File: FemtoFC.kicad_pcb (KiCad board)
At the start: 4 copper layers, 15 x 56 mm, 61 parts, among them J1 Power in, J3 Micro_SD_Card, J4 Pyro 2, J5 Pyro 2, P1 USB_C_Plug_USB2.0, Q1 FDS9926A, Q2 FDS4953, Q3 NDT3055L, U1 USBLC6-2SC6, U2 3.3v REG, U3 ATSAMD21G18A-M, U4 W25Q128JVS, U5 LSM6DS3, U6 BMP280

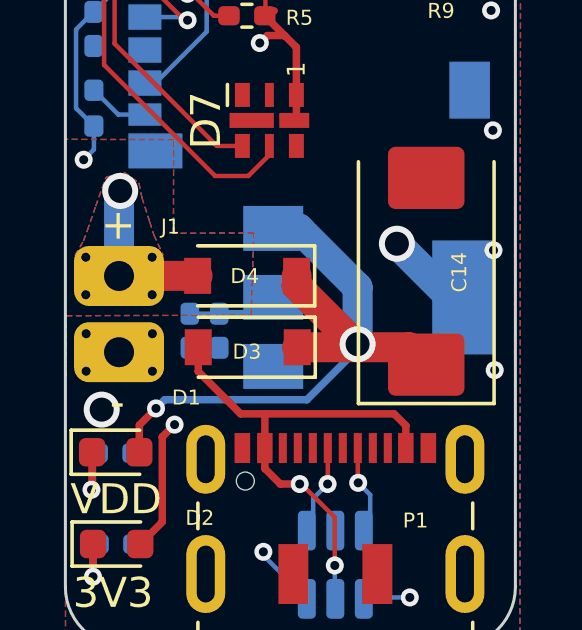
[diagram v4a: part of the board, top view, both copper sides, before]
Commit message: fixed ground short
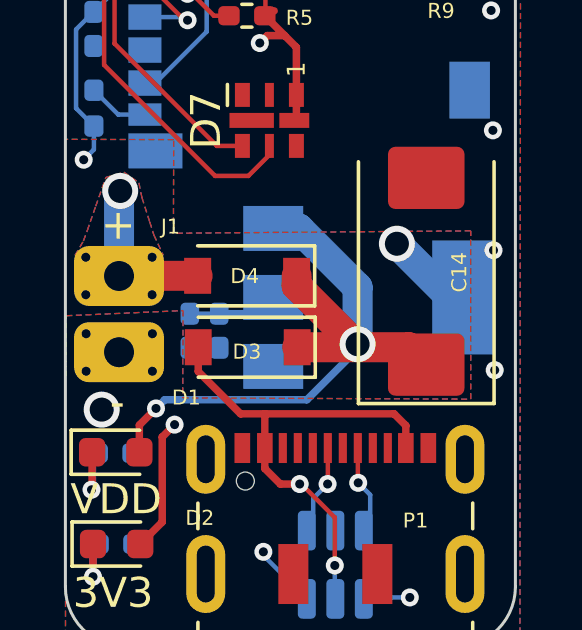
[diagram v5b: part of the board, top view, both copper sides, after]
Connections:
- C14 pad 1: GNDANA -> VDD
- D1 pad 2: GNDANA -> VDD
- D3 pad 1: GNDANA -> VDD
- D4 pad 1: GNDANA -> VDD
- U2 pad 3: GNDANA -> VDD
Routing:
- net VDD: track 0.00 -> 23.2 mm, vias 0 -> 2
- net GNDANA: track 25.7 -> 2.51 mm, vias 22 -> 20
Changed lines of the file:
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@@
   (net 68 "unconnected-(D7-Pad2)")
   (net 69 "unconnected-(D7-Pad3)")
+  (net 70 "VDD")
   (footprint "LED_SMD:LED_0603_1608Metric_Pad1.05x0.95mm_HandSolder" (layer "F.Cu")
     (at 81.22 46.62 -90)
@@
     (fp_line (start 1.4 -0.9) (end 1.4 0.9) (layer "F.Fab") (width 0.1))
     (pad "1" smd rect (at -1.65 0 180) (size 0.9 1.2) (layers "F.Cu" "F.Paste" "F.Mask")
-      (net 1 "GNDANA") (pinfunction "K") (pintype "passive"))
+      (net 70 "VDD") (pinfunction "K") (pintype "passive"))
     (pad "2" smd rect (at 1.65 0 180) (size 0.9 1.2) (layers "F.Cu" "F.Paste" "F.Mask")
       (net 6 "VBUS") (pinfunction "A") (pintype "passive"))
@@
     (fp_line (start -3.65 2.15) (end 3.65 2.15) (layer "F.Fab") (width 0.1))
     (pad "1" smd roundrect (at -3.1125 0 90) (size 2.075 2.55) (layers "F.Cu" "F.Paste" "F.Mask") (roundrect_rratio 0.1204819277)
-      (net 1 "GNDANA") (pintype "passive"))
+      (net 70 "VDD") (pintype "passive"))
     (pad "2" smd roundrect (at 3.1125 0 90) (size 2.075 2.55) (layers "F.Cu" "F.Paste" "F.Mask") (roundrect_rratio 0.1204819277)
       (net 1 "GNDANA") (pintype "passive"))
@@
     (fp_line (start -0.35 0) (end 0.25 -0.4) (layer "F.Fab") (width 0.1))
     (pad "1" smd rect (at -1.65 0 180) (size 0.9 1.2) (layers "F.Cu" "F.Paste" "F.Mask")
-      (net 1 "GNDANA") (pinfunction "K") (pintype "passive"))
+      (net 70 "VDD") (pinfunction "K") (pintype "passive"))
     (pad "2" smd rect (at 1.65 0 180) (size 0.9 1.2) (layers "F.Cu" "F.Paste" "F.Mask")
       (net 7 "+BATT") (pinfunction "A") (pintype "passive"))
@@
       (net 4 "Net-(D1-Pad1)") (pinfunction "K") (pintype "passive"))
     (pad "2" smd roundrect (at 0.7875 0) (size 0.875 0.95) (layers "F.Cu" "F.Paste" "F.Mask") (roundrect_rratio 0.25)
-      (net 1 "GNDANA") (pinfunction "A") (pintype "passive"))
+      (net 70 "VDD") (pinfunction "A") (pintype "passive"))
     (model "${KICAD6_3DMODEL_DIR}/LED_SMD.3dshapes/LED_0603_1608Metric.wrl"
       (offset (xyz 0 0 0))
@@
       (net 3 "VDDANA") (pinfunction "VO") (pintype "power_out"))
     (pad "3" smd rect (at -3.15 -2.3) (size 2 1.5) (layers "B.Cu" "B.Paste" "B.Mask")
-      (net 1 "GNDANA") (pinfunction "VI") (pintype "power_in"))
+      (net 70 "VDD") (pinfunction "VI") (pintype "power_in"))
     (model "${KICAD6_3DMODEL_DIR}/Package_TO_SOT_SMD.3dshapes/SOT-223.wrl"
       (offset (xyz 0 0 0))
@@
   )
   (segment (start 89.507521 55.28833) (end 89.507521 55.262479) (width 0.15) (layer "F.Cu") (net 1))
-  (segment (start 87.727857 84.01) (end 89.76 84.01) (width 1) (layer "F.Cu") (net 1))
   (segment (start 88.763006 50.274977) (end 88.53 50.507983) (width 0.15) (layer "F.Cu") (net 1))
   (segment (start 85.753056 56.053056) (end 85.753056 55.576944) (width 0.25) (layer "F.Cu") (net 1))
-  (segment (start 82.465357 86.604643) (end 82.465357 87.51) (width 0.25) (layer "F.Cu") (net 1))
-  (segment (start 87.707857 81.63) (end 87.707857 81.957857) (width 1) (layer "F.Cu") (net 1))
-  (segment (start 89.76 84.01) (end 91.447857 84.01) (width 1) (layer "F.Cu") (net 1))
   (segment (start 85.89 56.19) (end 85.753056 56.053056) (width 0.25) (layer "F.Cu") (net 1))
-  (segment (start 87.707857 81.957857) (end 89.76 84.01) (width 1) (layer "F.Cu") (net 1))
-  (segment (start 91.447857 84.01) (end 92.027857 84.59) (width 1) (layer "F.Cu") (net 1))
   (segment (start 86.413929 56.702544) (end 86.402544 56.702544) (width 0.25) (layer "F.Cu") (net 1))
   (segment (start 88.53 50.507983) (end 88.53 51.2525) (width 0.15) (layer "F.Cu") (net 1))
-  (segment (start 83.02 86.05) (end 82.465357 86.604643) (width 0.25) (layer "F.Cu") (net 1))
   (segment (start 86.402544 56.702544) (end 85.89 56.19) (width 0.25) (layer "F.Cu") (net 1))
   (via (at 93.91 39.3) (size 0.6) (drill 0.3) (layers "F.Cu" "B.Cu") (free) (net 1))
-  (via (at 83.02 86.05) (size 0.6) (drill 0.3) (layers "F.Cu" "B.Cu") (net 1))
   (via (at 81.09 39.24) (size 0.6) (drill 0.3) (layers "F.Cu" "B.Cu") (free) (net 1))
   (via (at 85.753056 55.576944) (size 0.8) (drill 0.4) (layers "F.Cu" "B.Cu") (net 1))
@@
   (via (at 94.25 76.78) (size 0.6) (drill 0.3) (layers "F.Cu" "B.Cu") (free) (net 1))
   (via (at 82.9 84.81) (size 0.6) (drill 0.3) (layers "F.Cu" "B.Cu") (net 1))
-  (via (at 89.74 83.91) (size 1.2) (drill 0.8) (layers "F.Cu" "B.Cu") (net 1))
-  (segment (start 87.776879 80.05) (end 86.927857 80.05) (width 1) (layer "B.Cu") (net 1))
-  (segment (start 83.02 86.05) (end 83.30952 85.76048) (width 0.25) (layer "B.Cu") (net 1))
-  (segment (start 89.74 82.013121) (end 87.776879 80.05) (width 1) (layer "B.Cu") (net 1))
-  (segment (start 83.30952 85.76048) (end 88.04952 85.76048) (width 0.25) (layer "B.Cu") (net 1))
-  (segment (start 86.580357 80.3975) (end 86.927857 80.05) (width 0.5) (layer "B.Cu") (net 1))
-  (segment (start 89.74 83.91) (end 89.74 82.013121) (width 1) (layer "B.Cu") (net 1))
-  (segment (start 88.04952 85.76048) (end 89.74 84.07) (width 0.25) (layer "B.Cu") (net 1))
-  (segment (start 89.74 84.07) (end 89.74 83.91) (width 0.25) (layer "B.Cu") (net 1))
   (segment (start 86.056097 57.056097) (end 84.38 55.38) (width 0.25) (layer "F.Cu") (net 2))
   (segment (start 84.38 55.38) (end 82.4275 55.38) (width 0.25) (layer "F.Cu") (net 2))
@@
   (segment (start 84.525 49.915) (end 84.525 51.655) (width 0.25) (layer "B.Cu") (net 67))
   (segment (start 91.755 47.101072) (end 91.755 46.725) (width 0.25) (layer "B.Cu") (net 67))
+  (segment (start 87.727857 84.01) (end 89.76 84.01) (width 1) (layer "F.Cu") (net 70))
+  (segment (start 82.465357 86.604643) (end 82.465357 87.51) (width 0.25) (layer "F.Cu") (net 70))
+  (segment (start 87.707857 81.63) (end 87.707857 81.957857) (width 1) (layer "F.Cu") (net 70))
+  (segment (start 89.76 84.01) (end 91.447857 84.01) (width 1) (layer "F.Cu") (net 70))
+  (segment (start 87.707857 81.957857) (end 89.76 84.01) (width 1) (layer "F.Cu") (net 70))
+  (segment (start 91.447857 84.01) (end 92.027857 84.59) (width 1) (layer "F.Cu") (net 70))
+  (segment (start 83.02 86.05) (end 82.465357 86.604643) (width 0.25) (layer "F.Cu") (net 70))
+  (via (at 83.02 86.05) (size 0.6) (drill 0.3) (layers "F.Cu" "B.Cu") (net 70))
+  (via (at 89.74 83.91) (size 1.2) (drill 0.8) (layers "F.Cu" "B.Cu") (net 70))
+  (segment (start 87.776879 80.05) (end 86.927857 80.05) (width 1) (layer "B.Cu") (net 70))
+  (segment (start 83.02 86.05) (end 83.30952 85.76048) (width 0.25) (layer "B.Cu") (net 70))
+  (segment (start 89.74 82.013121) (end 87.776879 80.05) (width 1) (layer "B.Cu") (net 70))
+  (segment (start 83.30952 85.76048) (end 88.04952 85.76048) (width 0.25) (layer "B.Cu") (net 70))
+  (segment (start 86.580357 80.3975) (end 86.927857 80.05) (width 0.5) (layer "B.Cu") (net 70))
+  (segment (start 89.74 83.91) (end 89.74 82.013121) (width 1) (layer "B.Cu") (net 70))
+  (segment (start 88.04952 85.76048) (end 89.74 84.07) (width 0.25) (layer "B.Cu") (net 70))
+  (segment (start 89.74 84.07) (end 89.74 83.91) (width 0.25) (layer "B.Cu") (net 70))
   (zone (net 7) (net_name "+BATT") (layers F&B.Cu) (hatch edge 0.508)
     (connect_pads yes (clearance 0.2))
@@
         (xy 80 94.27)
         (xy 80.03 82.96)
-        (xy 86.19 82.94)
-        (xy 86.28 80.2)
+        (xy 83.922604 82.788461)
+        (xy 83.910515 85.698144)
+        (xy 93.510369 85.740995)
+        (xy 93.509866 80.130091)
         (xy 83.6 80.21)
         (xy 83.61 77.09)

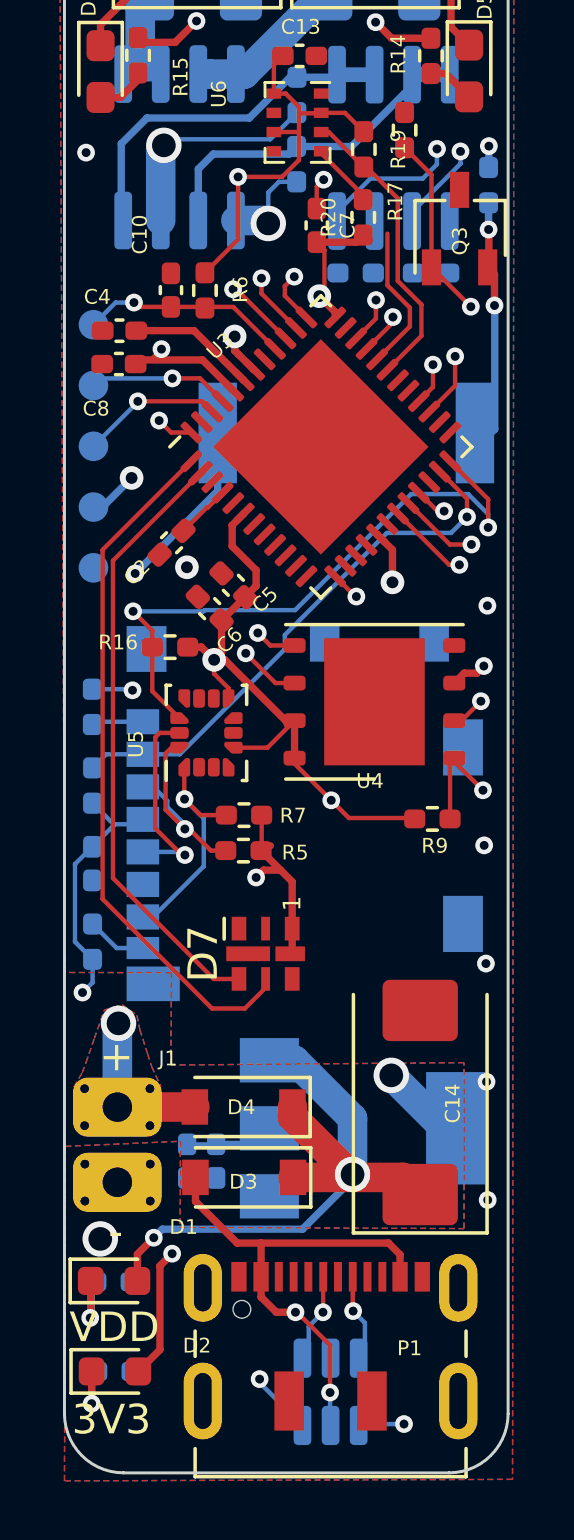
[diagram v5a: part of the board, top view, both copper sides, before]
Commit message: Shortcircuit fix, maybe final version before rev2
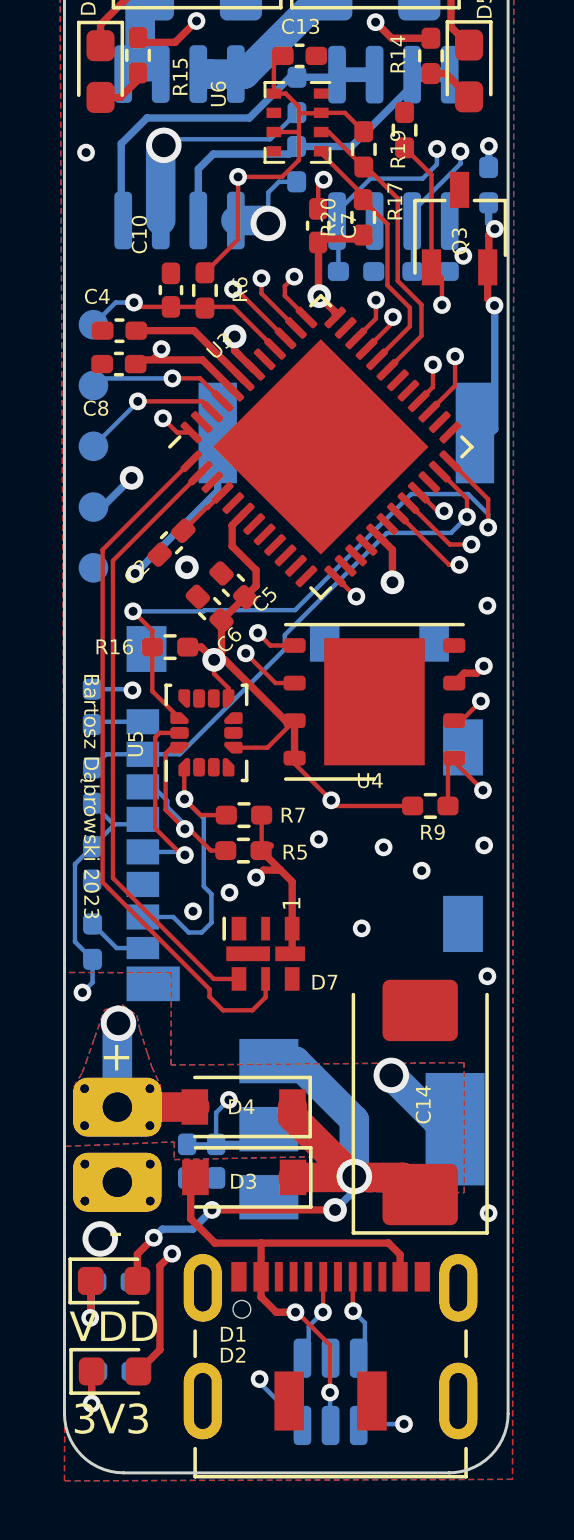
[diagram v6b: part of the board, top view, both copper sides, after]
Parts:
- R16: value 10k -> 100k
- moved R10 2.54 mm to (92.4, 53.4)
- moved R11 2.54 mm to (89.9, 53.4)
- moved R9 0.45 mm to (92.4, 71.5)
- moved C7 0.05 mm to (88.6, 51.8)
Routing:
- net MISO: track 23.5 -> 25.4 mm
- net P1_EN: track 14.7 -> 16.4 mm
- net P2_EN: track 16.1 -> 17.8 mm
- net SCL: track 7.25 -> 8.74 mm
- net VDDANA: track 76.2 -> 77.4 mm, vias 13 -> 14
- net VBUS: track 16.8 -> 17.3 mm
- net VDD: track 23.2 -> 23.6 mm, vias 2 -> 4
- net GNDANA: track 2.51 -> 2.50 mm, vias 20 -> 26
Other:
- board text added: "Bartosz Dąbrowski 2023"

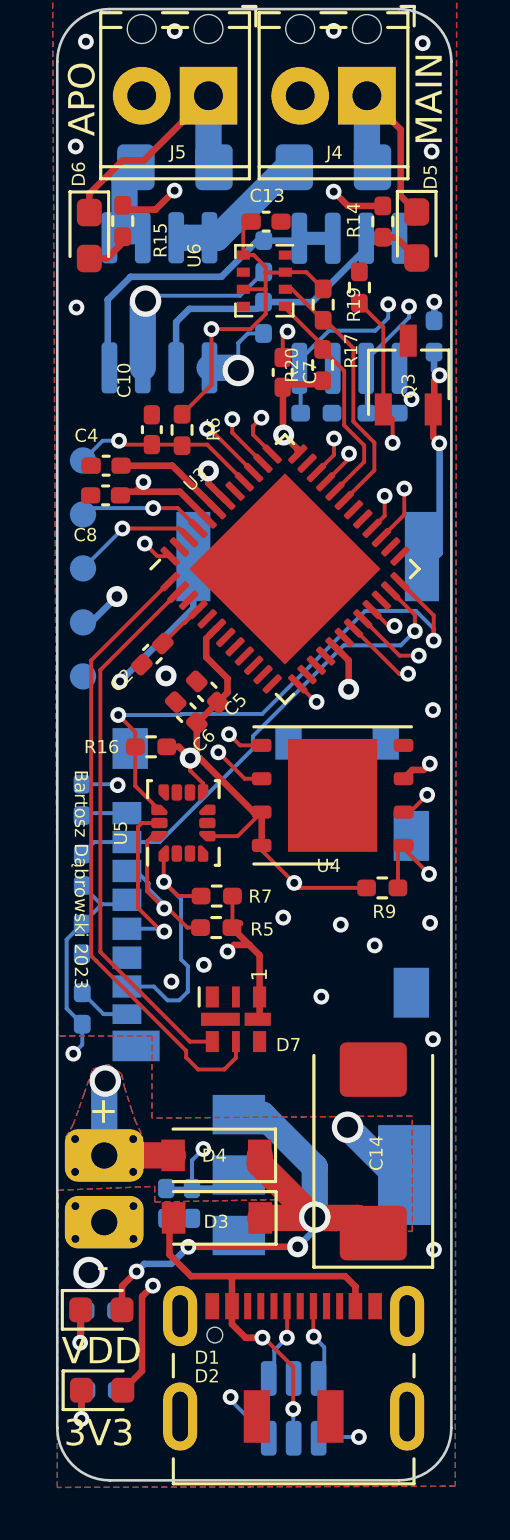
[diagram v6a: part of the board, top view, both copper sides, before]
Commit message: Removed a bunch of DRC warnings
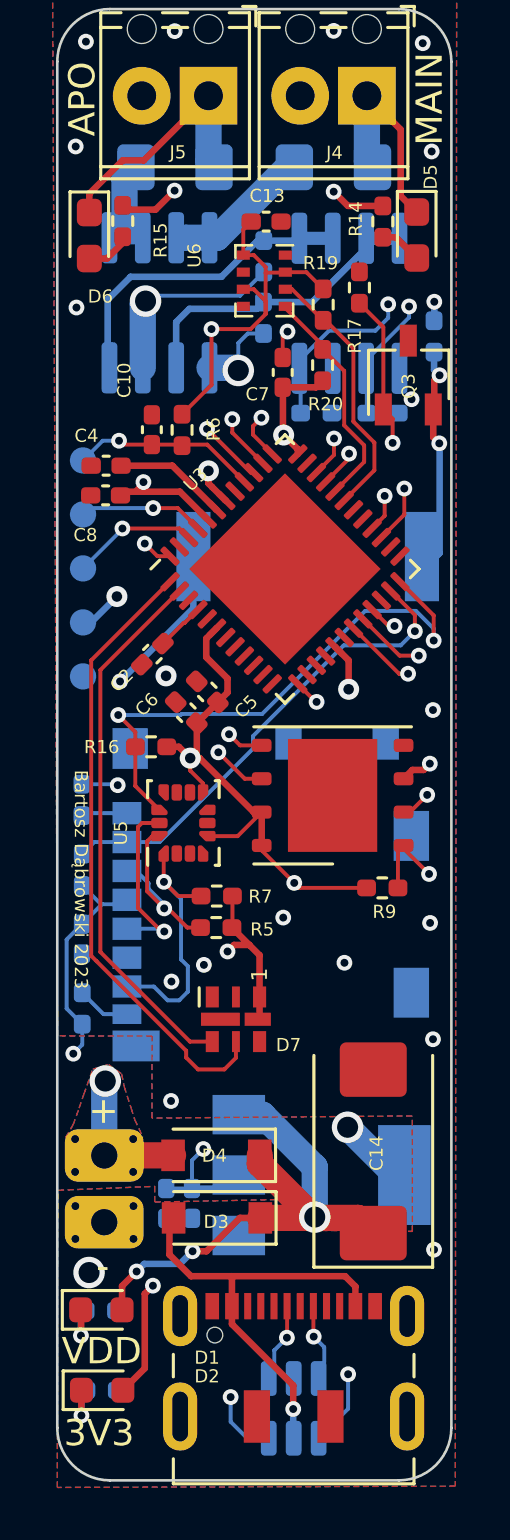
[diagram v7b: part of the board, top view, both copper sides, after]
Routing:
- net VDD: track 23.6 -> 20.6 mm, vias 4 -> 3
- net Net-(U1-Pad4): track 61.1 -> 62.7 mm
- net +BATT: track 83.3 -> 82.6 mm
- net Net-(D1-Pad1): track 2.56 -> 2.01 mm
- net VBUS: track 17.3 -> 16.9 mm, vias 2 -> 1
- net GNDANA: track 2.50 -> 2.47 mm, vias 26 -> 25
